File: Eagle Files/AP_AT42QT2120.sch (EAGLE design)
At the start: 20 parts, among them U2 AT42QT2120

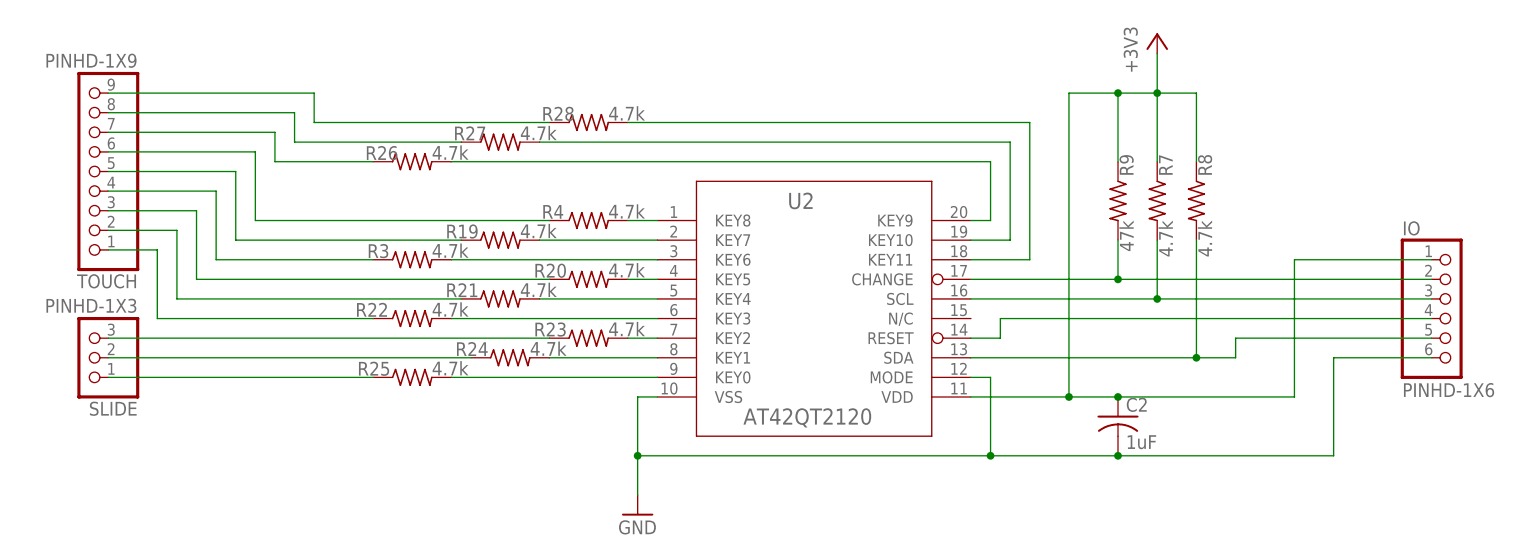
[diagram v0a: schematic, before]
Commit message: v2 with larger packages
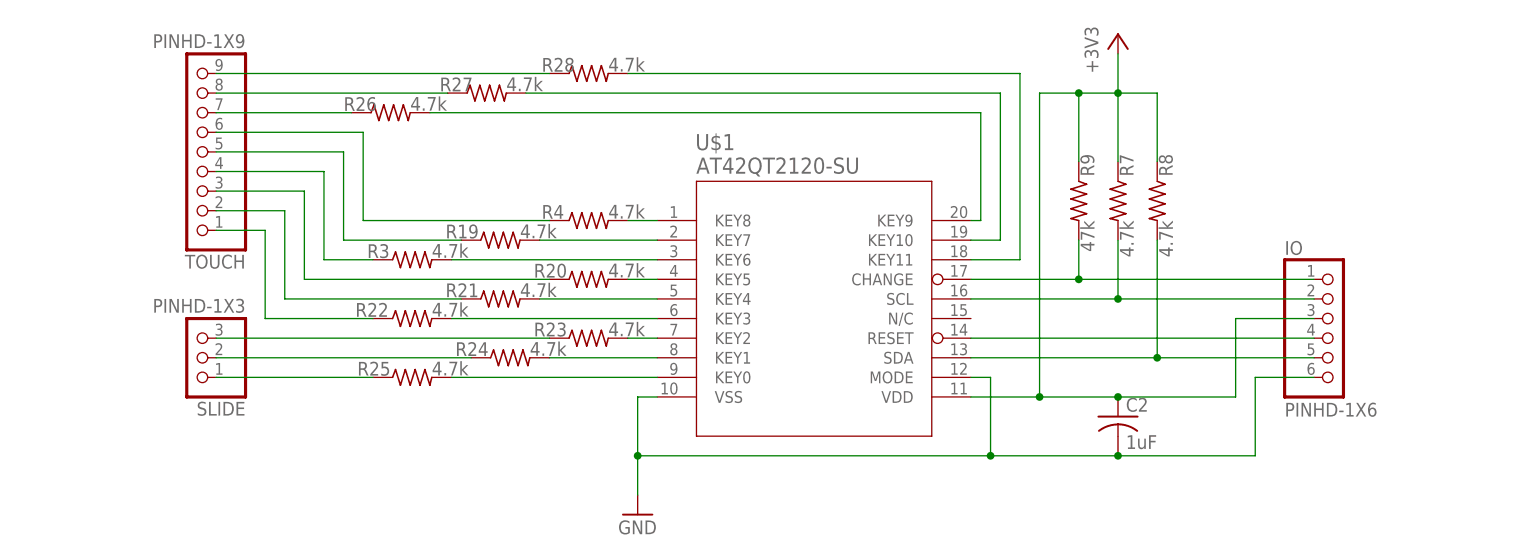
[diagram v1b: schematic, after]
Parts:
- removed U2: AT42QT2120, 2022-03-29_19-48-10_Library:AT42QT2120-XUTSSOP20_MC_MCH-L
- added U$1: AT42QT2120-SU, 2022-03-29_19-48-10_Library:AT42QT2120-SU
- C2: device rcl:C-USC0805 -> rcl:C-USC1206
- R19, R20, R21, R22, R23, R24, R25, R26, R27, R3, R4, R7, R8, R9: device rcl:R-US_R0805 -> rcl:R-US_R1206
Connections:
- removed net N$19 (its old number): R26.2, U2.KEY9
- removed net N$23: R27.2, U2.KEY10
- new net N$20: R26.2, U$1.KEY9
- new net N$29: R28.2, U$1.KEY11
- net +3V3: now also IO.3, U$1.VDD; no longer IO.1, U2.VDD
- net GND: now also U$1.MODE, U$1.VSS; no longer U2.MODE, U2.VSS
- net N$1: now also U$1.KEY8; no longer U2.KEY8
- net N$2: now also U$1.KEY7; no longer U2.KEY7
- net N$24: now also R27.2, U$1.KEY10; no longer R28.2, U2.KEY11
- net N$25: now also IO.2, U$1.SCL; no longer IO.3, U2.SCL
- net N$26: now also IO.1, U$1.CHANGE; no longer IO.2, U2.CHANGE
- net N$27: now also U$1.SDA; no longer U2.SDA
- net N$28: now also U$1.RESET; no longer U2.RESET
- net N$3: now also U$1.KEY6; no longer U2.KEY6
- net N$4: now also U$1.KEY5; no longer U2.KEY5
- net N$5: now also U$1.KEY4; no longer U2.KEY4
- net N$6: now also U$1.KEY3; no longer U2.KEY3
- net N$7: now also U$1.KEY2; no longer U2.KEY2
- net N$8: now also U$1.KEY1; no longer U2.KEY1
- net N$9: now also U$1.KEY0; no longer U2.KEY0
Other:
- moved on the sheet: IO, R26, R27, R28, R7, R8, R9, SLIDE, TOUCH
